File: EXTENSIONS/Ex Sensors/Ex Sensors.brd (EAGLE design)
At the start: 27 x 27 mm, 11 parts

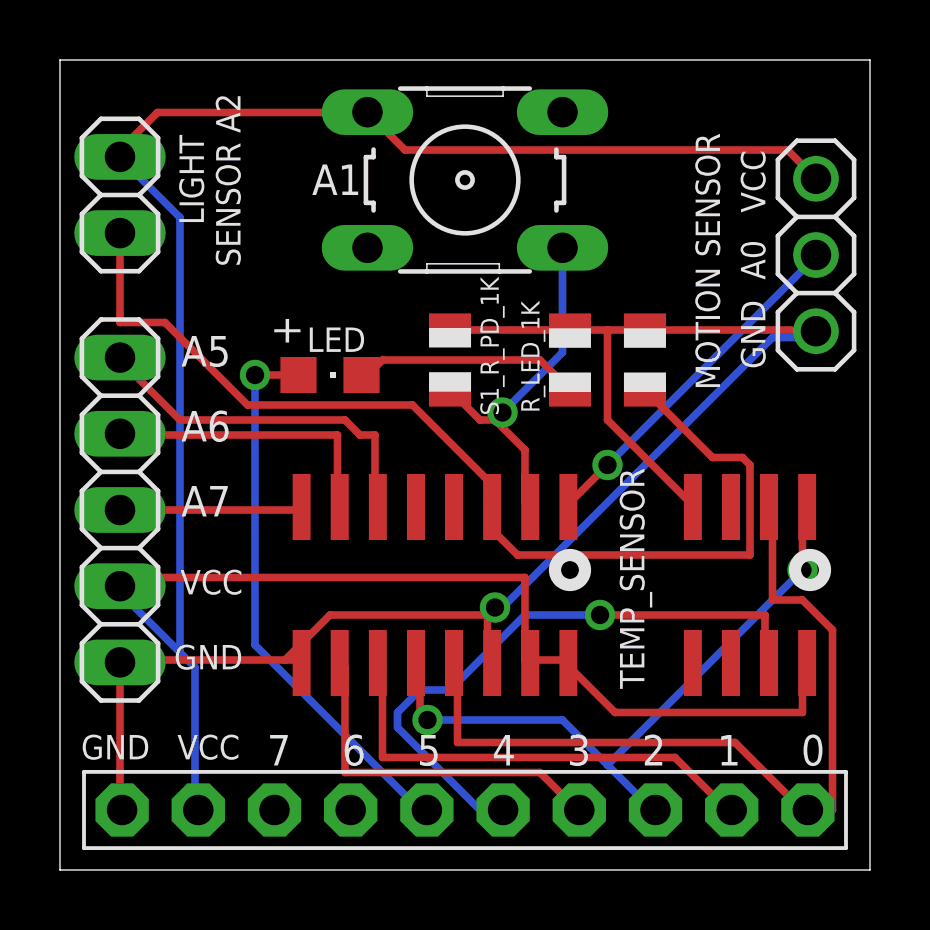
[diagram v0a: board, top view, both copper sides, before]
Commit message: Fix Nusbio gnd pin for gpios led resitor array
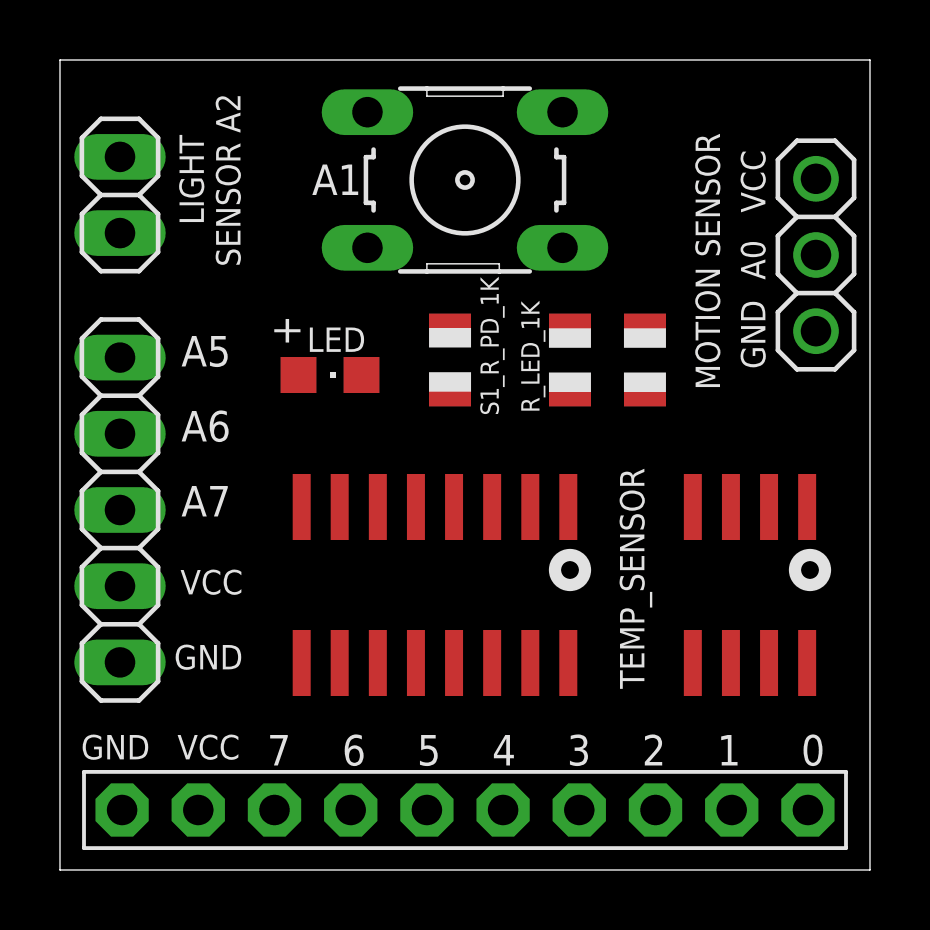
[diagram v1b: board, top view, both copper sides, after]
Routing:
- net VCC: track 79.0 -> 0.00 mm
- net GND: track 54.4 -> 0.00 mm, vias 1 -> 0
- net N$11: track 35.6 -> 0.00 mm
- net N$1: track 27.7 -> 0.00 mm
- net N$3: track 22.4 -> 0.00 mm, vias 2 -> 0
- net N$4: track 20.4 -> 0.00 mm, vias 1 -> 0
- net N$7: track 18.5 -> 0.00 mm, vias 1 -> 0
- net N$2: track 15.6 -> 0.00 mm
- net N$5: track 12.1 -> 0.00 mm
- net A5: track 12.0 -> 0.00 mm
- net N$12: track 12.0 -> 0.00 mm, vias 1 -> 0
- net N$10: track 11.9 -> 0.00 mm, vias 1 -> 0
- net A6: track 9.71 -> 0.00 mm
- net N$6: track 7.57 -> 0.00 mm
- net A7: track 6.11 -> 0.00 mm
